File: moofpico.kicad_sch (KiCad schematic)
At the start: 21 parts, among them J1 Serial, J2 Micro_SD_Card, J3 Bus_Apple_II_Card_Side, Q1 BS170, SW2 SW_DIP_x02, U1 Pico, U2 74LVC245, U3 74F11, U4 74LVC245, U5 74LVC245

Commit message: resync w/ libraries
add fp/sym for MEM2061

pretty sure I can't redistribute the MEM2061 footprints, alas
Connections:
- no-connect marks 32 -> 34
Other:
- moved on the sheet: F1, SW2
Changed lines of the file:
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@@
 	)
 	(junction
+		(at 170.18 29.21)
+		(diameter 0)
+		(color 0 0 0 0)
+	)
+	(junction
 		(at 110.49 171.45)
 		(diameter 0)
@@
 	)
 	(no_connect
+		(at 189.23 25.4)
+	)
+	(no_connect
 		(at 135.89 181.61)
 	)
@@
 	)
 	(no_connect
+		(at 173.99 25.4)
+	)
+	(no_connect
 		(at 161.29 179.07)
 	)
@@
 	(wire
 		(pts
-			(xy 184.15 27.94) (xy 186.69 27.94)
+			(xy 170.18 29.21) (xy 172.72 29.21)
+		)
+		(stroke
+			(width 0)
+			(type default)
+		)
+	)
+	(wire
+		(pts
+			(xy 189.23 27.94) (xy 191.77 27.94)
 		)
 		(stroke
@@
 	(wire
 		(pts
-			(xy 186.69 27.94) (xy 186.69 29.21)
+			(xy 191.77 27.94) (xy 191.77 29.21)
 		)
 		(stroke
@@
 	(wire
 		(pts
-			(xy 194.31 29.21) (xy 200.66 29.21)
-		)
-		(stroke
-			(width 0)
-			(type default)
-		)
-	)
-	(wire
-		(pts
 			(xy 166.37 57.15) (xy 173.99 57.15)
 		)
@@
 	(wire
 		(pts
-			(xy 167.64 27.94) (xy 168.91 27.94)
+			(xy 172.72 27.94) (xy 173.99 27.94)
 		)
 		(stroke
@@
 	(wire
 		(pts
-			(xy 167.64 27.94) (xy 167.64 29.21)
+			(xy 172.72 27.94) (xy 172.72 29.21)
 		)
 		(stroke
@@
 	(wire
 		(pts
-			(xy 167.64 29.21) (xy 166.37 29.21)
+			(xy 166.37 29.21) (xy 170.18 29.21)
 		)
 		(stroke
@@
 	(wire
 		(pts
+			(xy 199.39 29.21) (xy 200.66 29.21)
+		)
+		(stroke
+			(width 0)
+			(type default)
+		)
+	)
+	(wire
+		(pts
 			(xy 163.83 143.51) (xy 193.04 143.51)
 		)
@@
 	(wire
 		(pts
-			(xy 186.69 29.21) (xy 189.23 29.21)
+			(xy 191.77 29.21) (xy 194.31 29.21)
 		)
 		(stroke
@@
 	)
 	(symbol
+		(lib_id "power:PWR_FLAG")
+		(at 170.18 29.21 0)
+		(unit 1)
+		(exclude_from_sim no)
+		(in_bom yes)
+		(on_board yes)
+		(dnp no)
+		(property "Reference" "#FLG03"
+			(at 170.18 27.305 0)
+			(effects
+				(font
+					(size 1.27 1.27)
+				)
+				(hide yes)
+			)
+		)
+		(property "Value" "PWR_FLAG"
+			(at 168.402 24.384 0)
+			(effects
+				(font
+					(size 1.27 1.27)
+				)
+			)
+		)
+		(property "Footprint" ""
+			(at 170.18 29.21 0)
+			(effects
+				(font
+					(size 1.27 1.27)
+				)
+				(hide yes)
+			)
+		)
+		(property "Datasheet" "~"
+			(at 170.18 29.21 0)
+			(effects
+				(font
+					(size 1.27 1.27)
+				)
+				(hide yes)
+			)
+		)
+		(property "Description" "Special symbol for telling ERC where power comes from"
+			(at 170.18 29.21 0)
+			(effects
+				(font
+					(size 1.27 1.27)
+				)
+				(hide yes)
+			)
+		)
+		(pin "1"
+		)
+		(instances
+			(project "moofpico"
+				(path "/adf04048-7c47-4d7c-943c-c55ccf696419"
+					(reference "#FLG03")
+					(unit 1)
+				)
+			)
+		)
+	)
+	(symbol
 		(lib_id "power:GND")
 		(at 275.59 134.62 0)
@@
 	(symbol
 		(lib_id "Switch:SW_DIP_x02")
-		(at 176.53 27.94 0)
+		(at 181.61 27.94 0)
 		(mirror y)
 		(unit 1)
@@
 		(dnp no)
 		(property "Reference" "SW2"
-			(at 176.53 17.78 0)
+			(at 181.61 17.78 0)
 			(effects
 				(font
@@
 		)
 		(property "Value" "SW_DIP_x02"
-			(at 176.53 20.32 0)
+			(at 181.61 20.32 0)
 			(effects
 				(font
@@
 		)
 		(property "Footprint" "Button_Switch_THT:SW_DIP_SPSTx02_Slide_9.78x7.26mm_W7.62mm_P2.54mm"
-			(at 176.53 27.94 0)
+			(at 181.61 27.94 0)
 			(effects
 				(font
@@
 		)
 		(property "Datasheet" "https://www.mouser.com/datasheet/2/418/7/ENG_CD_1825360_B5-2021008.pdf"
-			(at 176.53 27.94 0)
+			(at 181.61 27.94 0)
 			(effects
 				(font
@@
 		)
 		(property "Description" "2x DIP Switch, Single Pole Single Throw (SPST) switch, small symbol"
-			(at 176.53 27.94 0)
+			(at 181.61 27.94 0)
 			(effects
 				(font
@@
 	(symbol
 		(lib_id "Device:Polyfuse_Small")
-		(at 191.77 29.21 90)
+		(at 196.85 29.21 90)
 		(unit 1)
 		(exclude_from_sim no)
@@
 		(on_board yes)
 		(dnp no)
-		(fields_autoplaced yes)
 		(property "Reference" "F1"
-			(at 191.77 22.86 90)
+			(at 196.85 22.86 90)
 			(effects
 				(font
@@
 		)
 		(property "Value" "60R050XUL"
-			(at 191.77 25.4 90)
+			(at 196.85 25.4 90)
 			(effects
 				(font
@@
 		)
 		(property "Footprint" "Fuse:Fuse_BelFuse_0ZRE0005FF_L8.3mm_W3.8mm"
-			(at 196.85 27.94 0)
+			(at 201.93 27.94 0)
 			(effects
 				(font
@@
 		)
 		(property "Datasheet" "~"
-			(at 191.77 29.21 0)
+			(at 196.85 29.21 0)
 			(effects
 				(font
@@
 		)
 		(property "Description" "Resettable fuse, polymeric positive temperature coefficient, small symbol"
-			(at 191.77 29.21 0)
+			(at 196.85 29.21 0)
 			(effects
 				(font

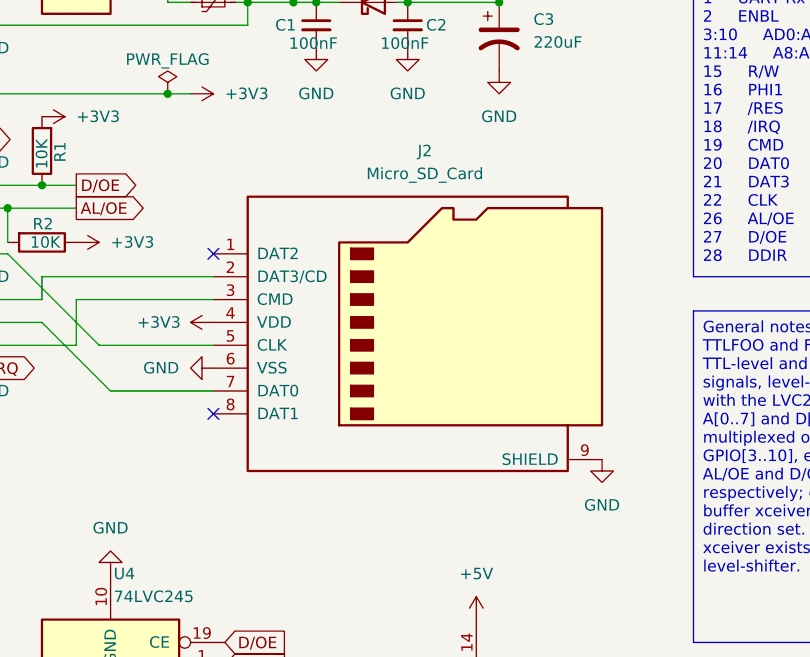
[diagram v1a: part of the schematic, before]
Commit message: use MEM2061 instead of "generic" SD
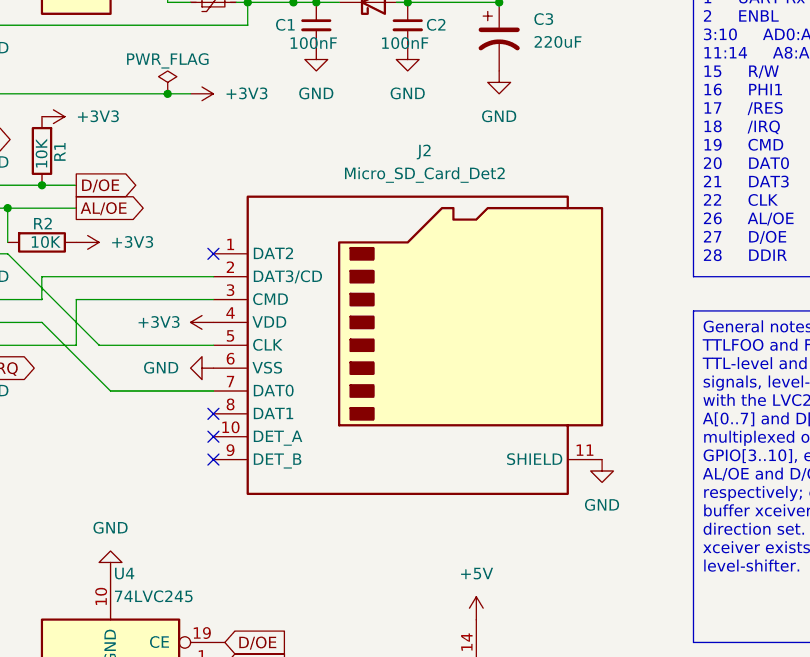
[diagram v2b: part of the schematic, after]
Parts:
- removed J2: Micro_SD_Card, Connector_Card:microSD_HC_Wuerth_693072010801, symbol Connector:Micro_SD_Card
- added J2: Micro_SD_Card_Det2, MEM2061_01_188_00_A:GCT_MEM2061-01-188-00-A_REVA, symbol Connector:Micro_SD_Card_Det2
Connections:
- net +3V3: now also J2.4 (VDD)
- net GND: now also J2.11 (SHIELD), J2.6 (VSS)
- net at U1.25 (GPIO19): now also J2.3 (CMD)
- net at U1.26 (GPIO20): now also J2.7 (DAT0)
- net at U1.27 (GPIO21): now also J2.2 (DAT3/CD)
- net at U1.29 (GPIO22): now also J2.5 (CLK)
- no-connect marks 34 -> 36
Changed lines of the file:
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@@
 	)
 	(no_connect
+		(at 196.85 80.01)
+	)
+	(no_connect
+		(at 196.85 77.47)
+	)
+	(no_connect
 		(at 151.13 189.23)
 	)
@@
 	)
 	(symbol
-		(lib_id "Connector:Micro_SD_Card")
-		(at 219.71 64.77 0)
-		(unit 1)
-		(exclude_from_sim no)
-		(in_bom yes)
-		(on_board yes)
-		(dnp no)
-		(fields_autoplaced yes)
-		(property "Reference" "J2"
-			(at 220.345 45.72 0)
-			(effects
-				(font
-					(size 1.27 1.27)
-				)
-			)
-		)
-		(property "Value" "Micro_SD_Card"
-			(at 220.345 48.26 0)
-			(effects
-				(font
-					(size 1.27 1.27)
-				)
-			)
-		)
-		(property "Footprint" "Connector_Card:microSD_HC_Wuerth_693072010801"
-			(at 248.92 57.15 0)
-			(effects
-				(font
-					(size 1.27 1.27)
-				)
-				(hide yes)
-			)
-		)
-		(property "Datasheet" "http://katalog.we-online.de/em/datasheet/693072010801.pdf"
-			(at 219.71 64.77 0)
-			(effects
-				(font
-					(size 1.27 1.27)
-				)
-				(hide yes)
-			)
-		)
-		(property "Description" "Micro SD Card Socket"
-			(at 219.71 64.77 0)
-			(effects
-				(font
-					(size 1.27 1.27)
-				)
-				(hide yes)
-			)
-		)
-		(pin "2"
-		)
-		(pin "3"
-		)
-		(pin "5"
-		)
-		(pin "6"
-		)
-		(pin "1"
-		)
-		(pin "7"
-		)
-		(pin "8"
-		)
-		(pin "4"
-		)
-		(pin "9"
-		)
-		(instances
-			(project "moofpico"
-				(path "/adf04048-7c47-4d7c-943c-c55ccf696419"
-					(reference "J2")
-					(unit 1)
-				)
-			)
-		)
-	)
-	(symbol
 		(lib_id "power:GND")
 		(at 76.2 34.29 180)
@@
 					(unit 1)
 				)
+			)
+		)
+	)
+	(symbol
+		(lib_id "Connector:Micro_SD_Card_Det2")
+		(at 219.71 67.31 0)
+		(unit 1)
+		(exclude_from_sim no)
+		(in_bom yes)
+		(on_board yes)
+		(dnp no)
+		(fields_autoplaced yes)
+		(property "Reference" "J2"
+			(at 220.345 45.72 0)
+			(effects
+				(font
+					(size 1.27 1.27)
+				)
+			)
+		)
+		(property "Value" "Micro_SD_Card_Det2"
+			(at 220.345 48.26 0)
+			(effects
+				(font
+					(size 1.27 1.27)
+				)
+			)
+		)
+		(property "Footprint" "MEM2061_01_188_00_A:GCT_MEM2061-01-188-00-A_REVA"
+			(at 271.78 49.53 0)
+			(effects
+				(font
+					(size 1.27 1.27)
+				)
+				(hide yes)
+			)
+		)
+		(property "Datasheet" "https://www.hirose.com/en/product/document?clcode=&productname=&series=DM3&documenttype=Catalog&lang=en&documentid=D49662_en"
+			(at 222.25 64.77 0)
+			(effects
+				(font
+					(size 1.27 1.27)
+				)
+				(hide yes)
+			)
+		)
+		(property "Description" "Micro SD Card Socket with two card detection pins"
+			(at 219.71 67.31 0)
+			(effects
+				(font
+					(size 1.27 1.27)
+				)
+				(hide yes)
+			)
+		)
+		(pin "8"
+		)
+		(pin "9"
+		)
+		(pin "5"
+		)
+		(pin "3"
+		)
+		(pin "1"
+		)
+		(pin "7"
+		)
+		(pin "11"
+		)
+		(pin "2"
+		)
+		(pin "6"
+		)
+		(pin "4"
+		)
+		(pin "10"
+		)
+		(instances
+			(project "moofpico"
+				(path "/adf04048-7c47-4d7c-943c-c55ccf696419"
+					(reference "J2")
+					(unit 1)
+				)

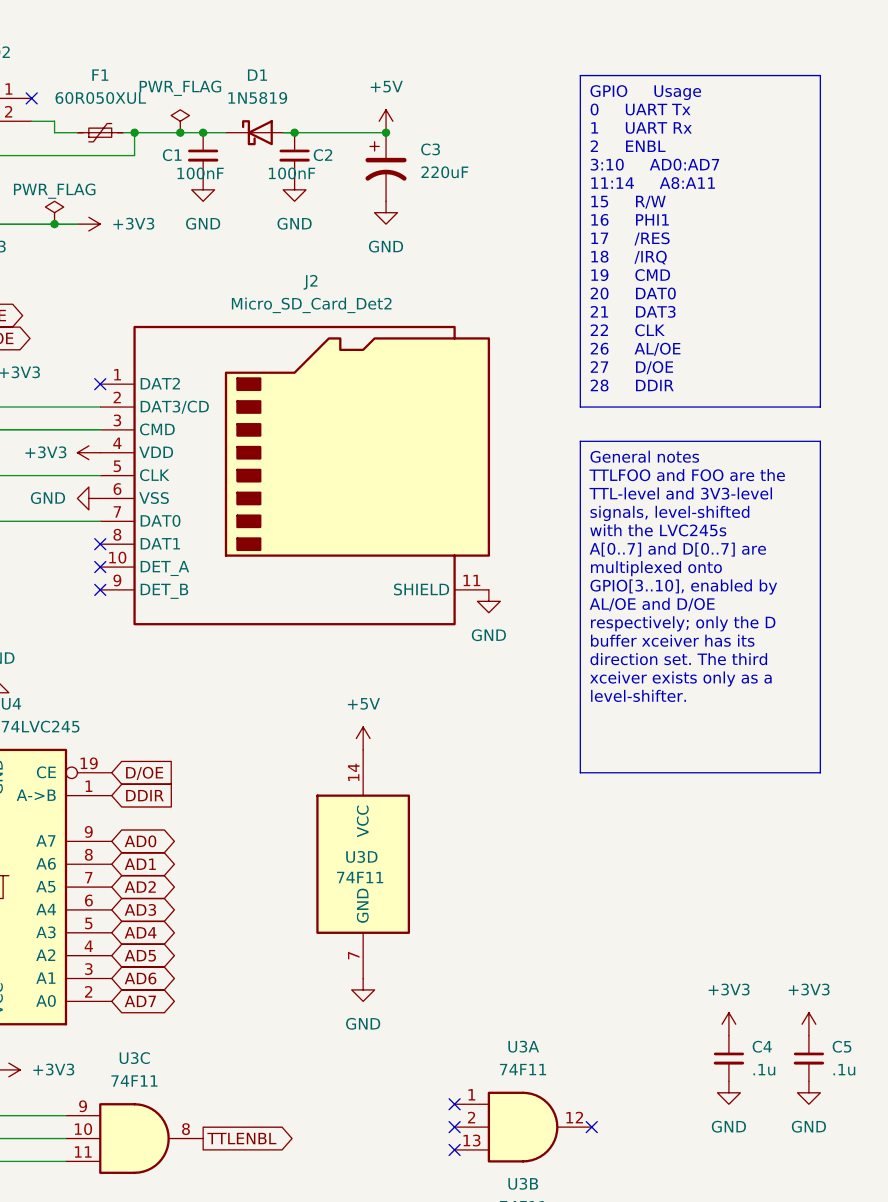
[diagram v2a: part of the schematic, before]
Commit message: make +3V3 and GND a little thicker; move +3V3 trace out from between some other RPi traces and onto its own test point/header pin/quasi-via
faffing about with power and ground

but *why*?
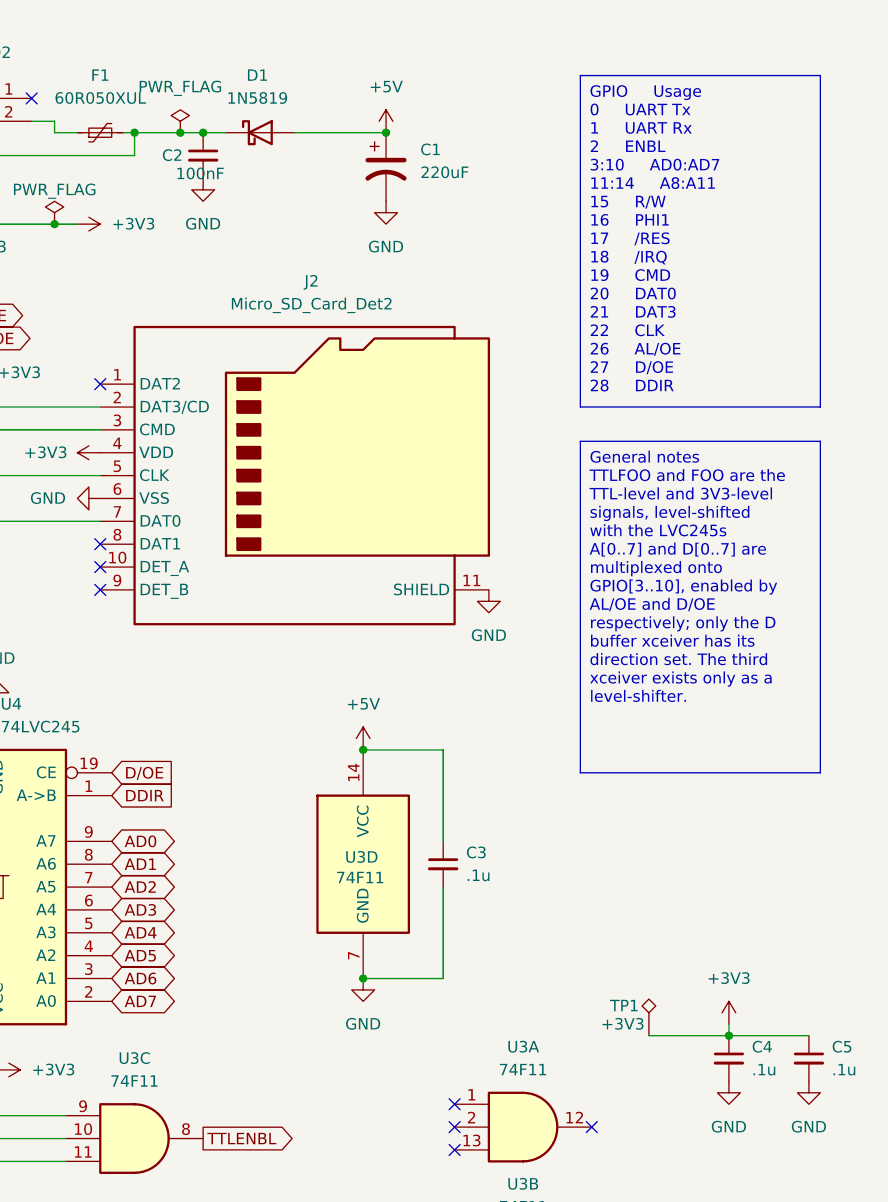
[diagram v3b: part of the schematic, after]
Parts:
- removed C2: 100nF, Capacitor_THT:C_Disc_D3.0mm_W1.6mm_P2.50mm, symbol Device:C_Small
- added C3: .1u, Capacitor_THT:C_Disc_D3.8mm_W2.6mm_P2.50mm, symbol Device:C_Small
- added TP1: +3V3, Connector_PinHeader_1.00mm:PinHeader_1x01_P1.00mm_Vertical, symbol Connector:TestPoint_Alt
- renumbered C3 to C1, C1 to C2
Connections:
- net +3V3: now also TP1.1
- net +5V: now also C3.1
- net GND: now also C3.2

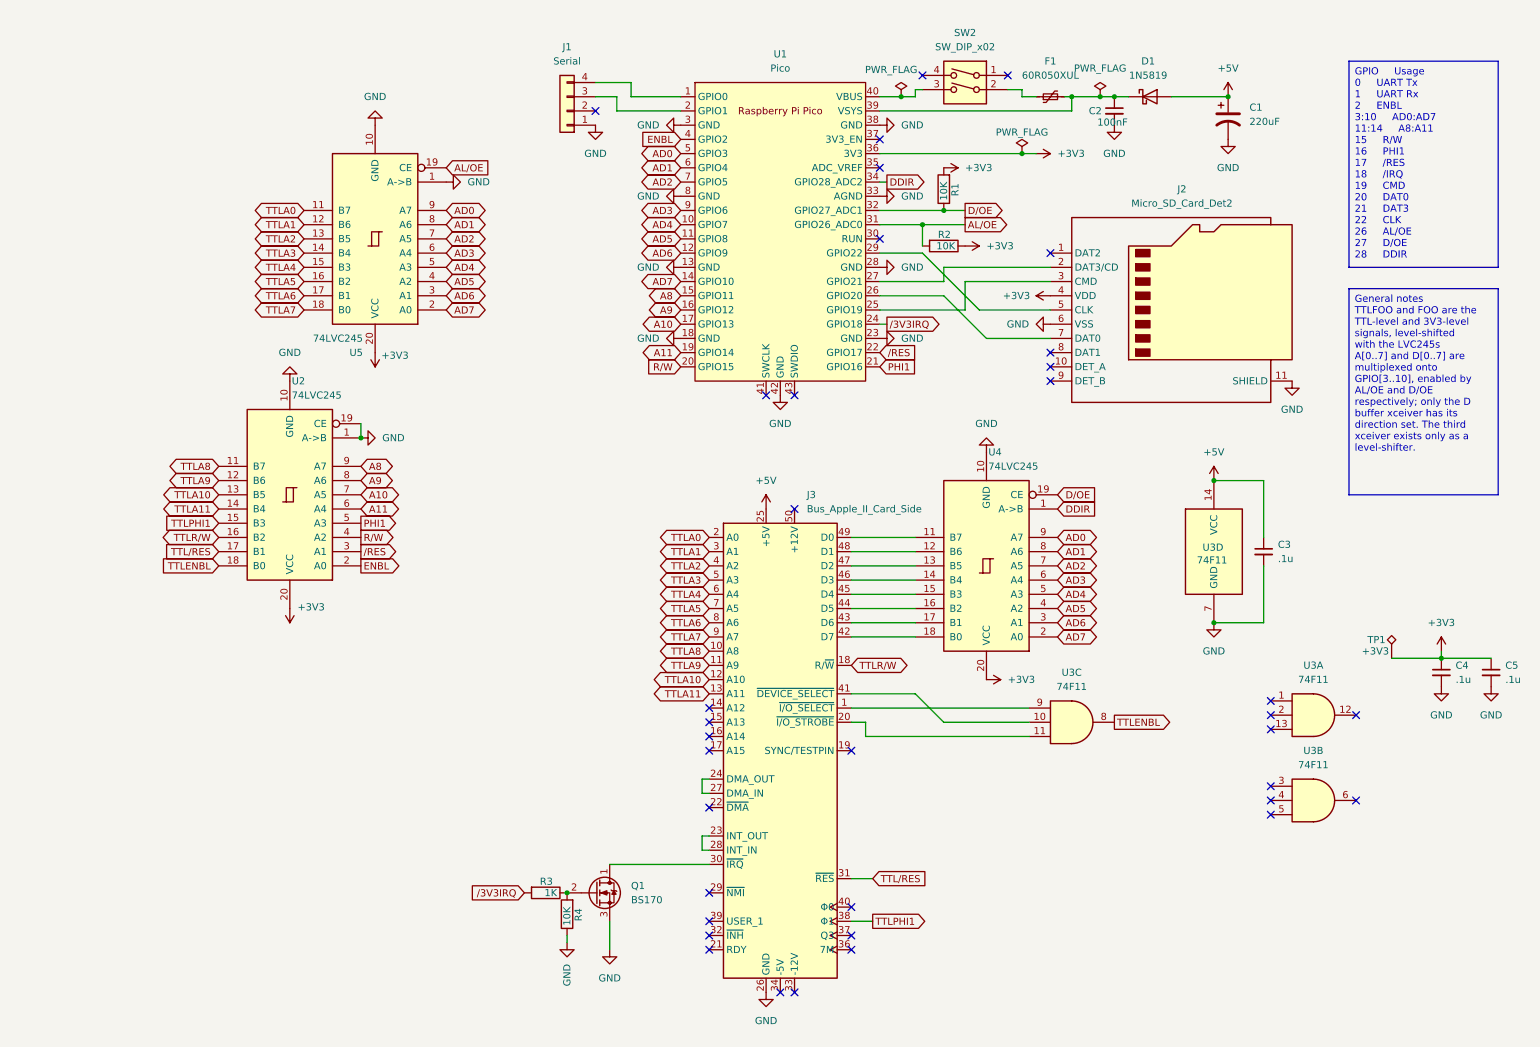
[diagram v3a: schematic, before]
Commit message: update datasheet URLs; add extra shield pin to uSD
more accurately specify capacitor size

nudged rpi over so that it sat on the mill grid

more footprint futzing

move to 5 pin serial/power connector
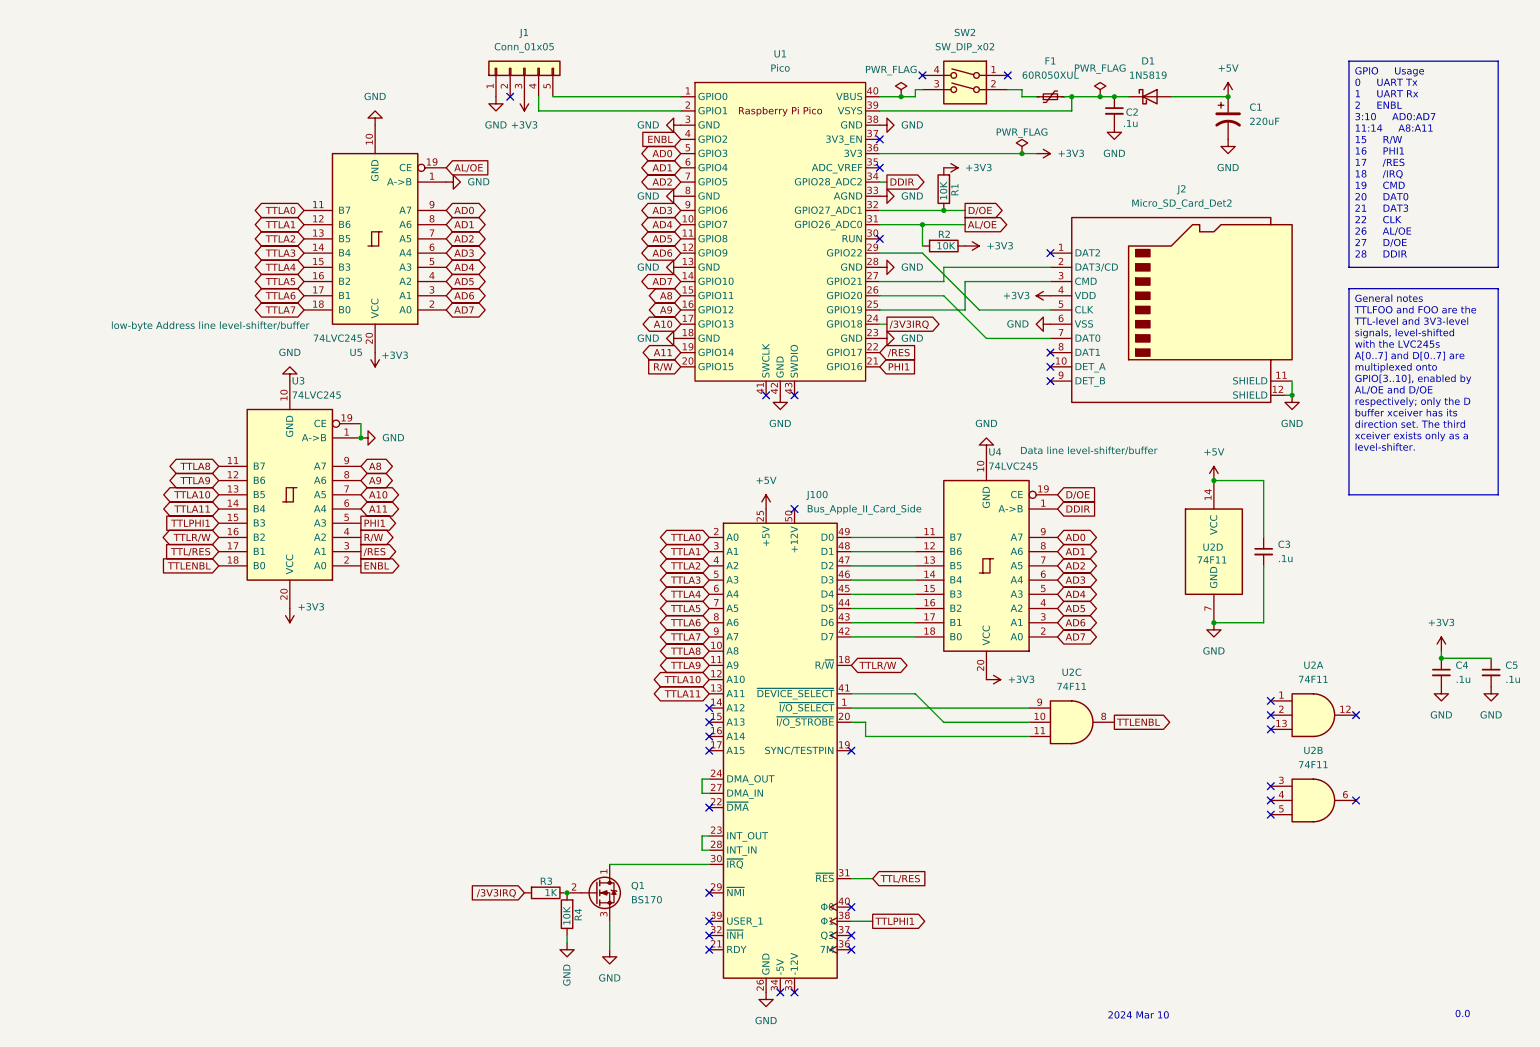
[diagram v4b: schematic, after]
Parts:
- removed J1: Serial, Connector:NS-Tech_Grove_1x04_P2mm_Vertical, symbol Connector_Generic:Conn_01x04
- removed TP1: +3V3, Connector_PinHeader_1.00mm:PinHeader_1x01_P1.00mm_Vertical, symbol Connector:TestPoint_Alt
- added J1: Conn_01x05, Connector_PinSocket_2.00mm:PinSocket_1x05_P2.00mm_Vertical, symbol Connector_Generic:Conn_01x05
- C1: footprint Capacitor_THT:CP_Radial_D10.0mm_P5.00mm -> Capacitor_THT:CP_Radial_D6.3mm_P2.50mm
- C2: value 100nF -> .1u; footprint Capacitor_THT:C_Disc_D3.0mm_W1.6mm_P2.50mm -> Capacitor_THT:C_Disc_D3.8mm_W2.6mm_P2.50mm
- renumbered J3 to J100, U3 to U2, U2 to U3
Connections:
- net +3V3: now also J1.3 (Pin_3)
- net GND: now also J2.12 (SHIELD), J1.1 (Pin_1)
- net at U1.1 (GPIO0): now also J1.5 (Pin_5)
- net at U1.2 (GPIO1): now also J1.4 (Pin_4)
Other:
- note added: "0.0"
- note added: "2024 Mar 10"
